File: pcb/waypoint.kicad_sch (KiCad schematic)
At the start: 47 parts, among them M1 LD0832AA-0126F, SW1 L, SW2 OK, SW3 R, U1 BX-PH2.0-2PWZ, U10 TCA9534PWR, U2 GT-USB-7010ASV, U3 USBLC6-2SC6_C5261088, U4 DRV2605LDGST, U5 ESP32-C6-WROOM-1-N8, U6 240x240 SPI, U7 ATGM336H-5NR-32, U8 LSM6DS3TR-C, U9 IIS2MDCTR

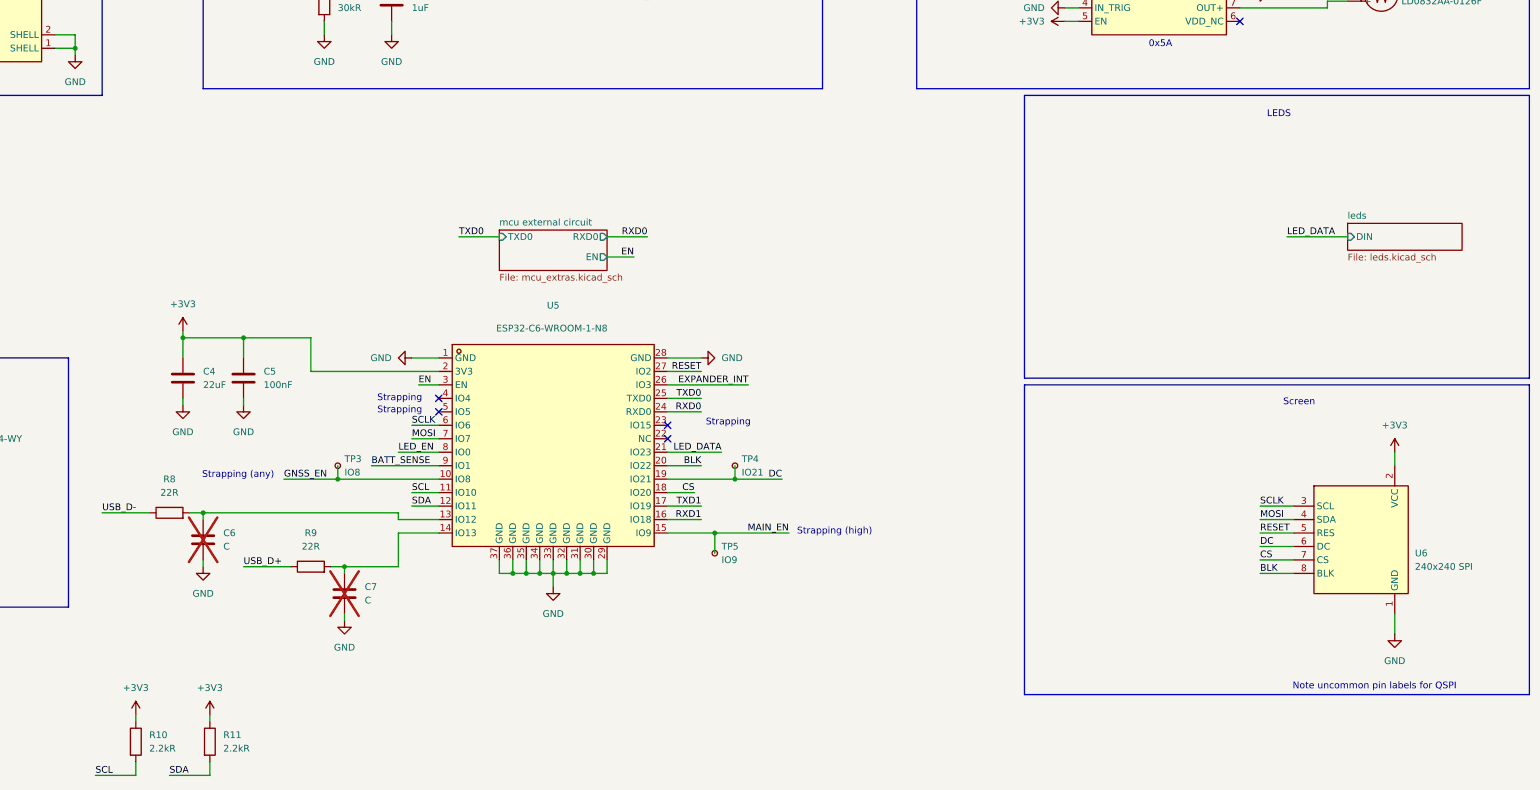
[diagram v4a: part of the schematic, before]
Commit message: Started with firmware, missing display, navigation and leds
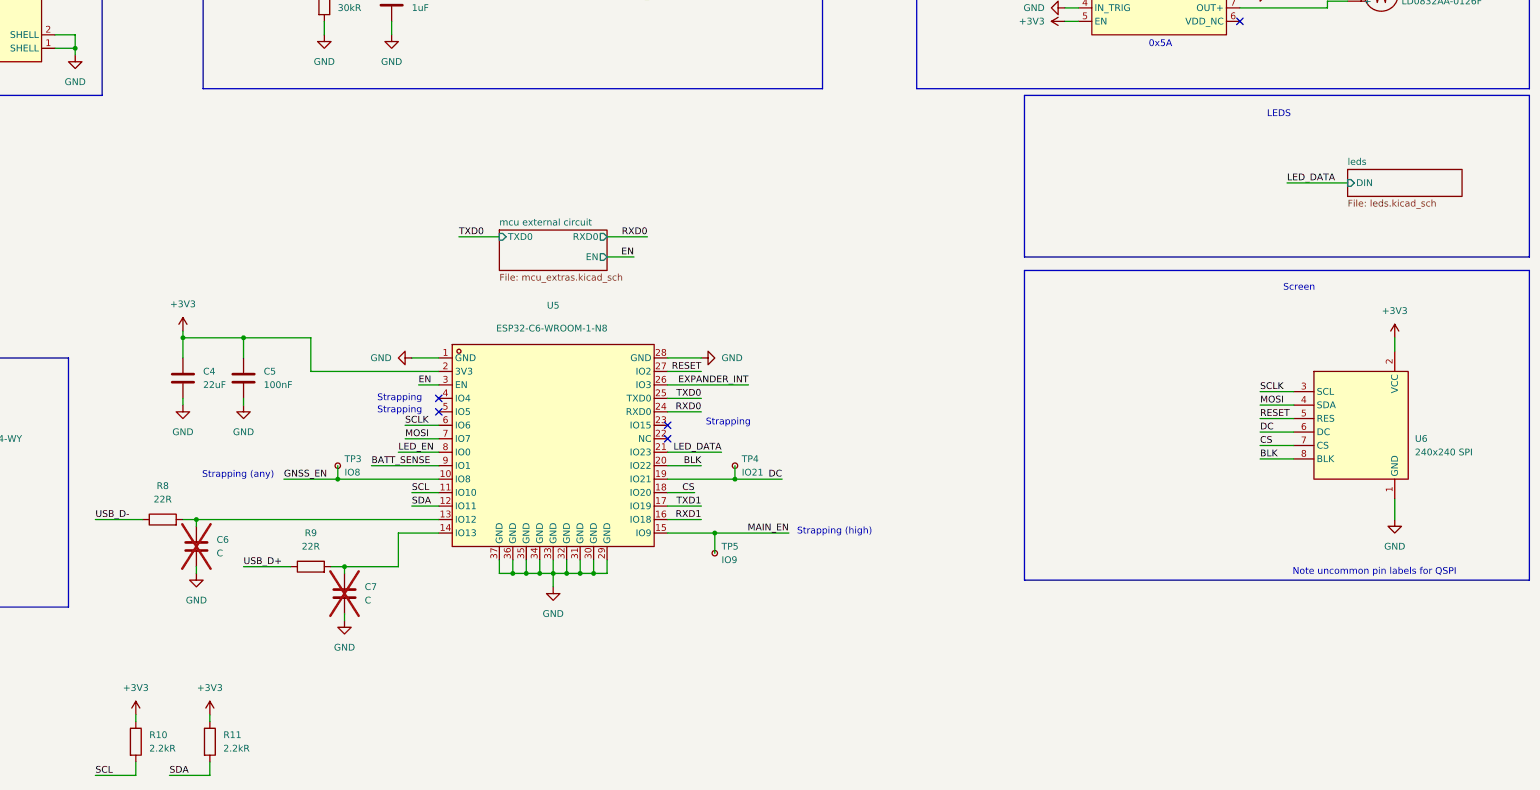
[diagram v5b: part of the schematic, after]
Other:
- moved on the sheet: C6, R8, U6
